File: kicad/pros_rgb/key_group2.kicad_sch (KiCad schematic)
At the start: 8 parts

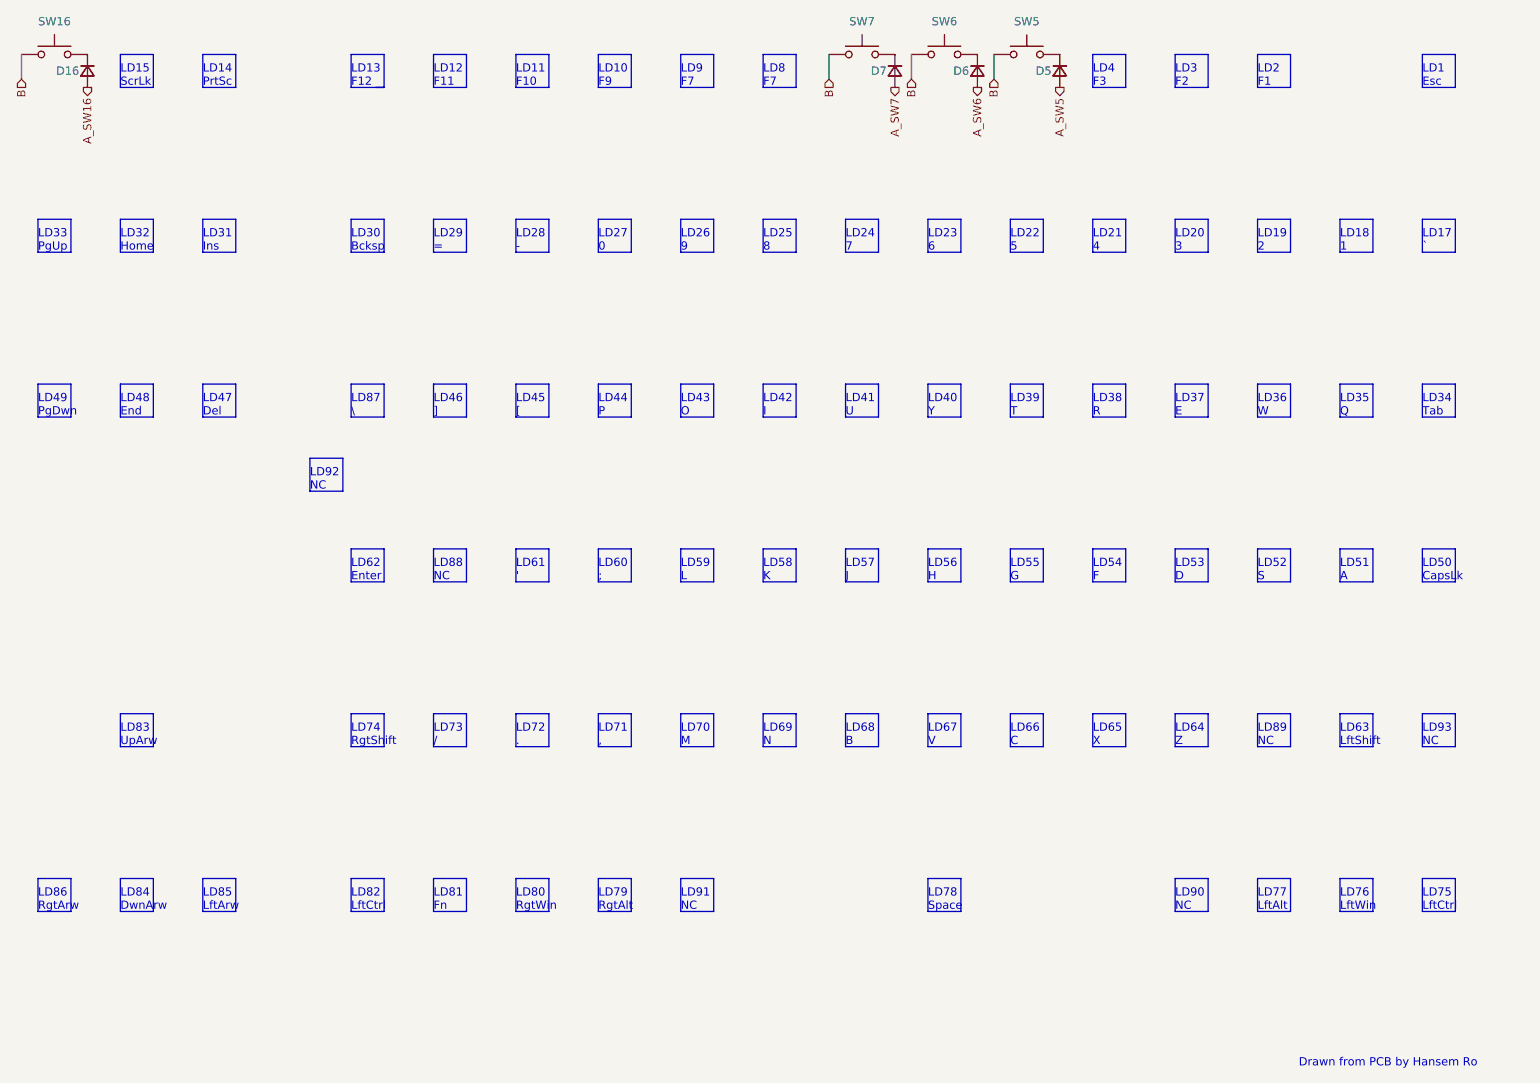
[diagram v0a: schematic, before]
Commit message: kicad/pros_rgb: update key groupings
These new groupings are based off ordering in firmware:
https://github.com/hansemro/pok3r_re_firmware/blob/4b68aa4baf7d28dc8dbf8eebcb1fdb59e7bcd629/disassemble/cmprosrgb/v122/cmprosrgb_v122.txt#L14599-L14629
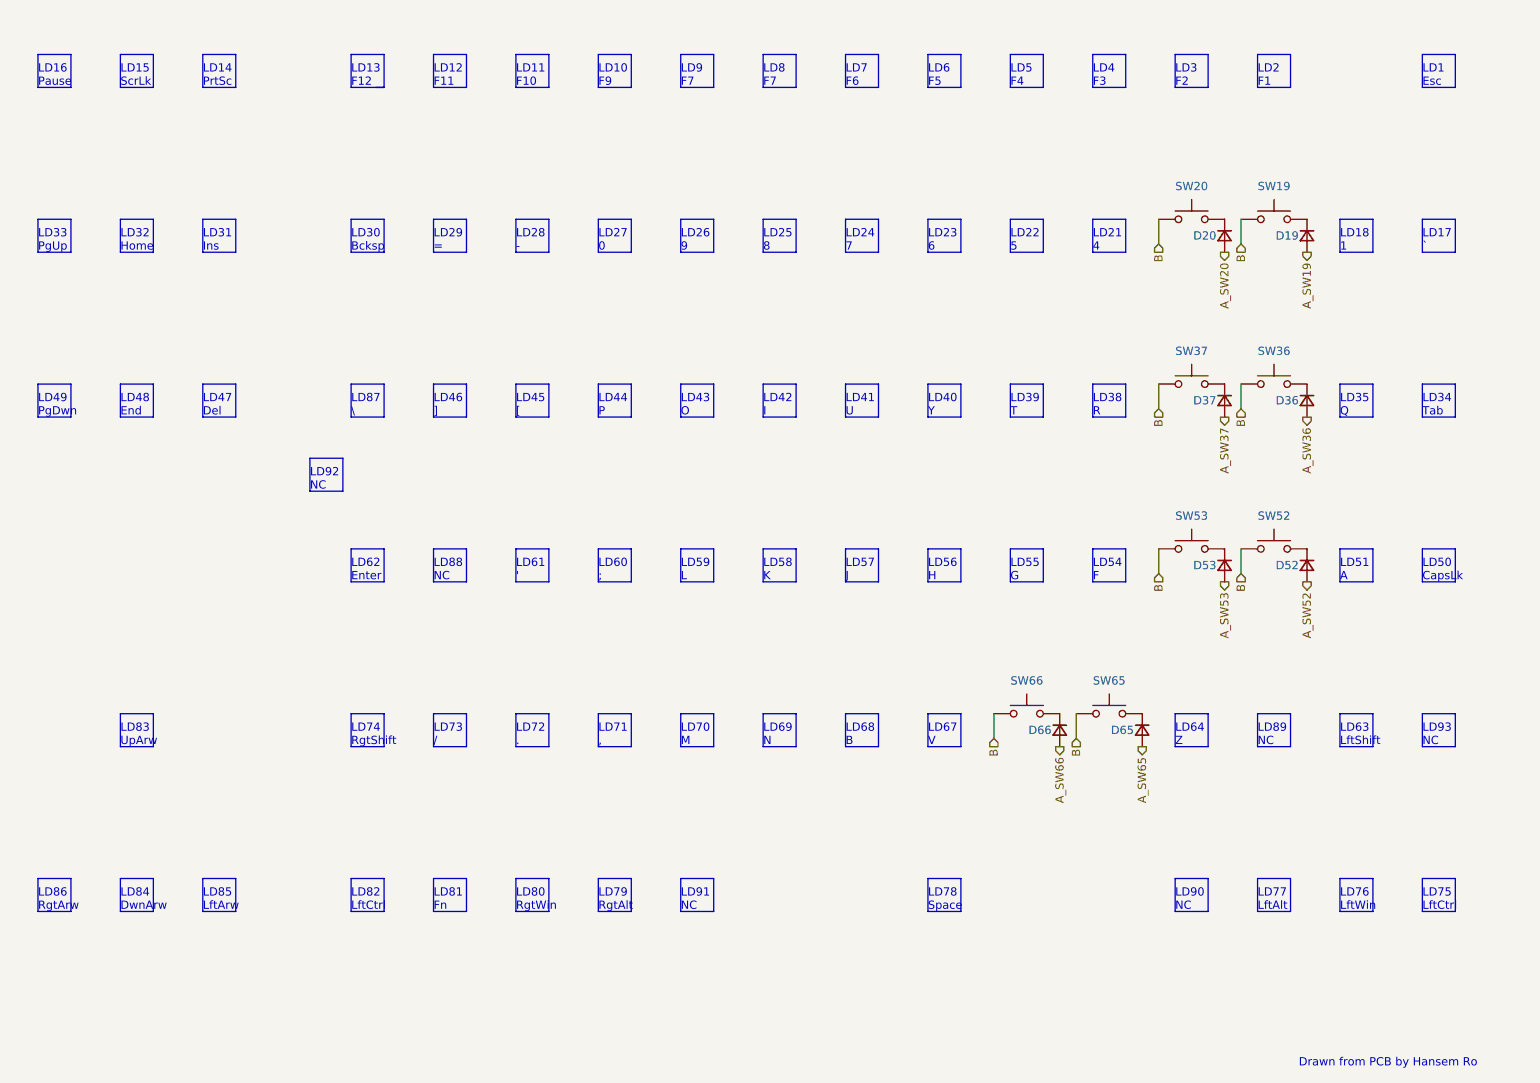
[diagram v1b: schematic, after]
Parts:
- removed D16, D5, D6, D7: ~, symbol Device:D_Small
- removed SW16, SW5, SW6, SW7: ~, symbol Switch:SW_Push
- added D19, D20, D36, D37, D52, D53, D65, D66: (no value), symbol Device:D_Small
- added SW19, SW20, SW36, SW37, SW52, SW53, SW65, SW66: (no value), symbol Switch:SW_Push
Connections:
- net B: now also SW19.1, SW20.1, SW36.1, SW37.1, SW52.1, SW53.1, SW65.1, SW66.1
- new net: D53.1 (K), SW53.2
- new net: D36.1 (K), SW36.2
- new net: D52.1 (K), SW52.2
- new net: D65.1 (K), SW65.2
- new net: D20.1 (K), SW20.2
- new net: D37.1 (K), SW37.2
- new net: D66.1 (K), SW66.2
- new net: D19.1 (K), SW19.2
- new net A_SW19: D19.2 (A)
- new net A_SW20: D20.2 (A)
- new net A_SW36: D36.2 (A)
- new net A_SW37: D37.2 (A)
- new net A_SW52: D52.2 (A)
- new net A_SW53: D53.2 (A)
- new net A_SW65: D65.2 (A)
- new net A_SW66: D66.2 (A)
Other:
- note added: "LD16 Pause"
- note added: "LD5 F4"
- note added: "LD6 F5"
- note added: "LD7 F6"
- note removed: "LD19 2"
- note removed: "LD20 3"
- note removed: "LD36 W"
- note removed: "LD37 E"
- note removed: "LD52 S"
- note removed: "LD53 D"
- note removed: "LD65 X"
- note removed: "LD66 C"

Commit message: kicad/pros_rgb: mark as Rev. B
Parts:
- D19, D20, D36, D37, D52, D53, D65, D66, SW19, SW20, SW36, SW37, SW52, SW53, SW65, SW66: value (none) -> ~
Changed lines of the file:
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@@
     (in_bom yes) (on_board yes)
     (property "Reference" "SW53" (id 0) (at 236.22 95.25 0))
-    (property "Value" "" (id 1) (at 236.22 95.25 0))
+    (property "Value" "~" (id 1) (at 236.22 95.25 0))
     (property "Footprint" "" (id 2) (at 236.22 95.25 0)
       (effects (font (size 1.27 1.27)) hide)
@@
       (effects (font (size 1.27 1.27)) (justify right))
     )
-    (property "Value" "" (id 1) (at 256.54 78.7399 90)
+    (property "Value" "~" (id 1) (at 256.54 78.7399 90)
       (effects (font (size 1.27 1.27)) (justify left))
     )
@@
       (effects (font (size 1.27 1.27)) (justify right))
     )
-    (property "Value" "" (id 1) (at 256.54 104.1399 90)
+    (property "Value" "~" (id 1) (at 256.54 104.1399 90)
       (effects (font (size 1.27 1.27)) (justify left))
     )
@@
       (effects (font (size 1.27 1.27)) (justify right))
     )
-    (property "Value" "" (id 1) (at 231.14 129.5399 90)
+    (property "Value" "~" (id 1) (at 231.14 129.5399 90)
       (effects (font (size 1.27 1.27)) (justify left))
     )
@@
       (effects (font (size 1.27 1.27)) (justify right))
     )
-    (property "Value" "" (id 1) (at 243.84 53.3399 90)
+    (property "Value" "~" (id 1) (at 243.84 53.3399 90)
       (effects (font (size 1.27 1.27)) (justify left))
     )
@@
     (in_bom yes) (on_board yes)
     (property "Reference" "SW36" (id 0) (at 248.92 69.85 0))
-    (property "Value" "" (id 1) (at 248.92 69.85 0))
+    (property "Value" "~" (id 1) (at 248.92 69.85 0))
     (property "Footprint" "" (id 2) (at 248.92 69.85 0)
       (effects (font (size 1.27 1.27)) hide)
@@
     (in_bom yes) (on_board yes)
     (property "Reference" "SW37" (id 0) (at 236.22 69.85 0))
-    (property "Value" "" (id 1) (at 236.22 69.85 0))
+    (property "Value" "~" (id 1) (at 236.22 69.85 0))
     (property "Footprint" "" (id 2) (at 236.22 69.85 0)
       (effects (font (size 1.27 1.27)) hide)
@@
     (in_bom yes) (on_board yes)
     (property "Reference" "SW66" (id 0) (at 210.82 120.65 0))
-    (property "Value" "" (id 1) (at 210.82 120.65 0))
+    (property "Value" "~" (id 1) (at 210.82 120.65 0))
     (property "Footprint" "" (id 2) (at 210.82 120.65 0)
       (effects (font (size 1.27 1.27)) hide)
@@
       (effects (font (size 1.27 1.27)) (justify right))
     )
-    (property "Value" "" (id 1) (at 243.84 78.7399 90)
+    (property "Value" "~" (id 1) (at 243.84 78.7399 90)
       (effects (font (size 1.27 1.27)) (justify left))
     )
@@
     (in_bom yes) (on_board yes)
     (property "Reference" "SW19" (id 0) (at 248.92 44.45 0))
-    (property "Value" "" (id 1) (at 248.92 44.45 0))
+    (property "Value" "~" (id 1) (at 248.92 44.45 0))
     (property "Footprint" "" (id 2) (at 248.92 44.45 0)
       (effects (font (size 1.27 1.27)) hide)
@@
       (effects (font (size 1.27 1.27)) (justify right))
     )
-    (property "Value" "" (id 1) (at 256.54 53.3399 90)
+    (property "Value" "~" (id 1) (at 256.54 53.3399 90)
       (effects (font (size 1.27 1.27)) (justify left))
     )
@@
     (in_bom yes) (on_board yes)
     (property "Reference" "SW20" (id 0) (at 236.22 44.45 0))
-    (property "Value" "" (id 1) (at 236.22 44.45 0))
+    (property "Value" "~" (id 1) (at 236.22 44.45 0))
     (property "Footprint" "" (id 2) (at 236.22 44.45 0)
       (effects (font (size 1.27 1.27)) hide)
@@
       (effects (font (size 1.27 1.27)) (justify right))
     )
-    (property "Value" "" (id 1) (at 243.84 104.1399 90)
+    (property "Value" "~" (id 1) (at 243.84 104.1399 90)
       (effects (font (size 1.27 1.27)) (justify left))
     )
@@
     (in_bom yes) (on_board yes)
     (property "Reference" "SW52" (id 0) (at 248.92 95.25 0))
-    (property "Value" "" (id 1) (at 248.92 95.25 0))
+    (property "Value" "~" (id 1) (at 248.92 95.25 0))
     (property "Footprint" "" (id 2) (at 248.92 95.25 0)
       (effects (font (size 1.27 1.27)) hide)
@@
     (in_bom yes) (on_board yes)
     (property "Reference" "SW65" (id 0) (at 223.52 120.65 0))
-    (property "Value" "" (id 1) (at 223.52 120.65 0))
+    (property "Value" "~" (id 1) (at 223.52 120.65 0))
     (property "Footprint" "" (id 2) (at 223.52 120.65 0)
       (effects (font (size 1.27 1.27)) hide)
@@
       (effects (font (size 1.27 1.27)) (justify right))
     )
-    (property "Value" "" (id 1) (at 218.44 129.5399 90)
-      (effects (font (size 1.27 1.27)) (justify left))
-    )
+    (property "Value" "~" (id 1) (at 218.44 129.5399 90)
+      (effects (font (size 1.27 1.27)) (justify left))
+    )

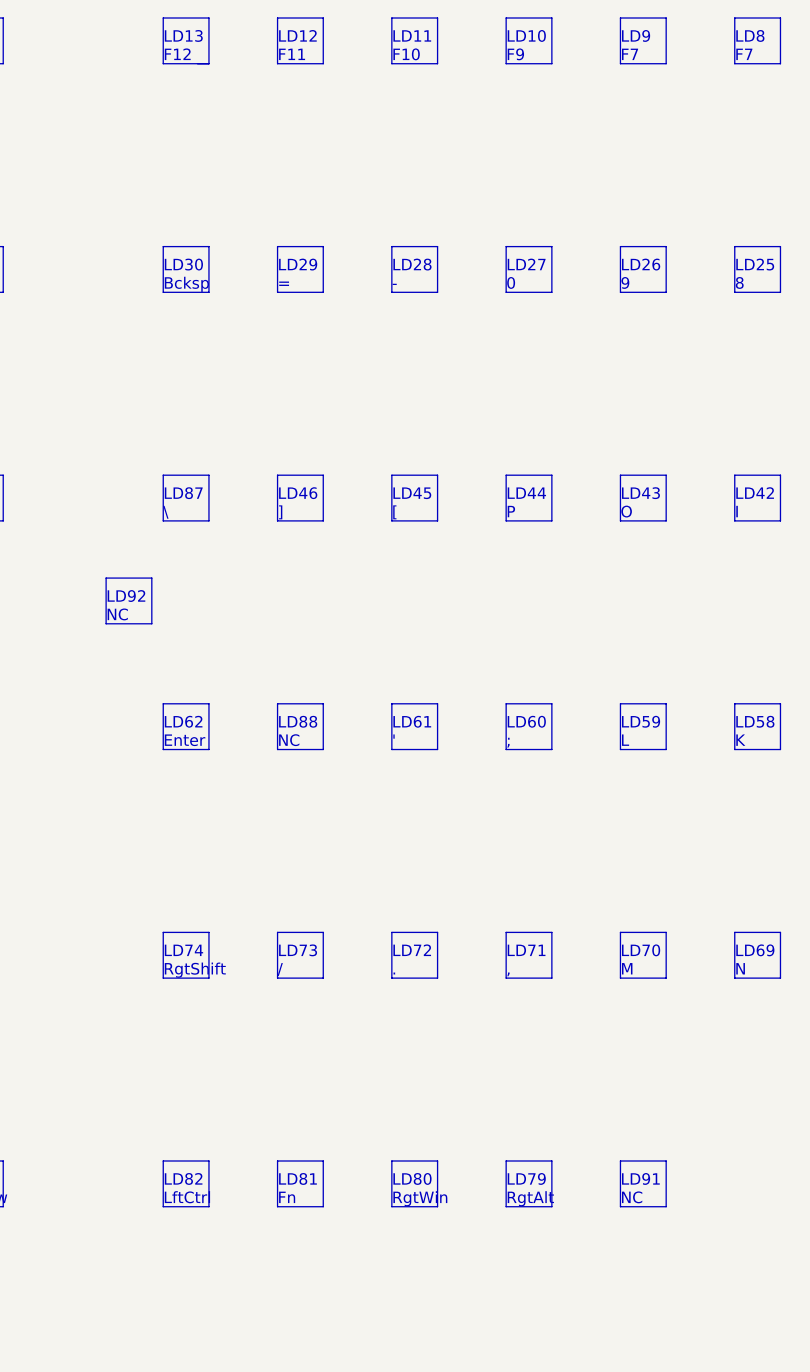
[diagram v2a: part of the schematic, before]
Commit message: kicad/pros_rgb: fix typos
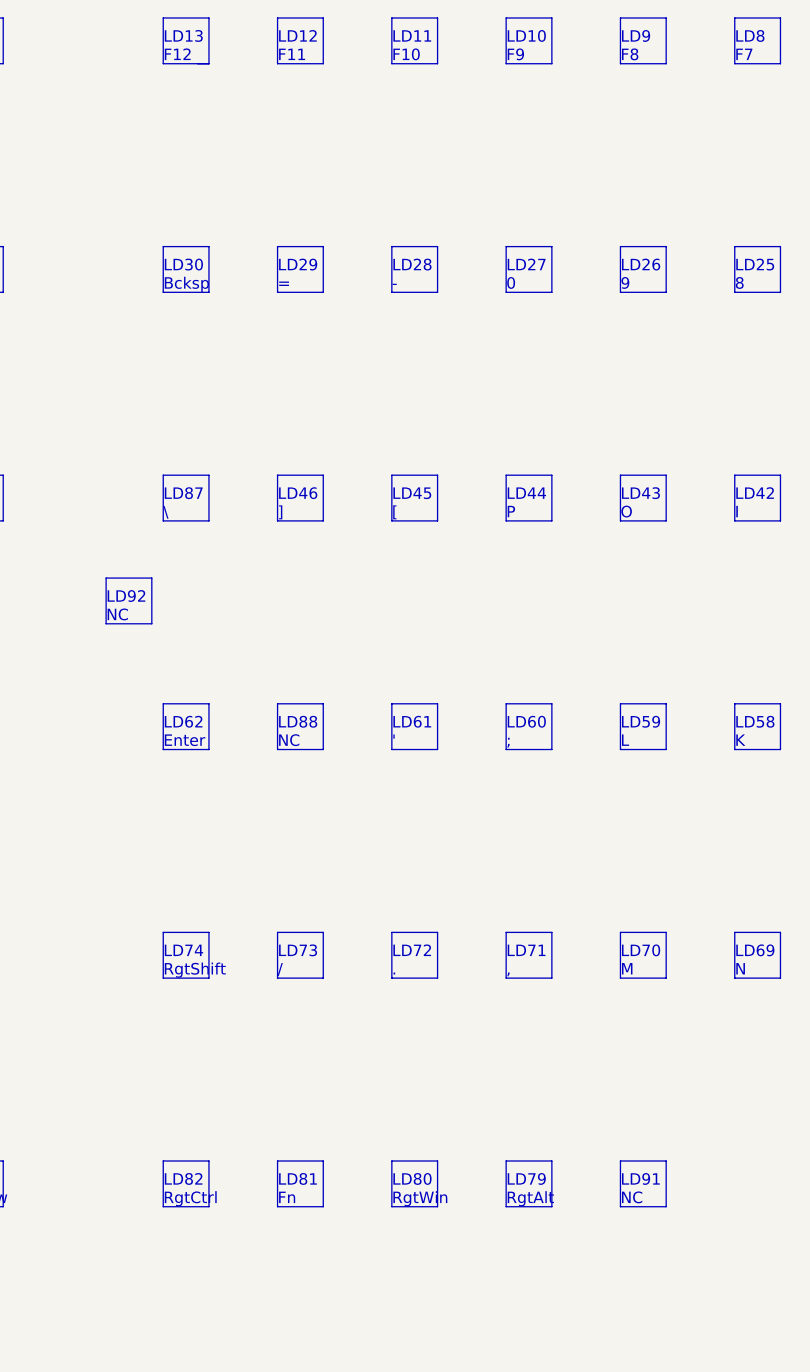
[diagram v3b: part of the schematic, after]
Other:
- note added: "LD82 RgtCtrl"
- note added: "LD9 F8"
- note removed: "LD82 LftCtrl"
- note removed: "LD9 F7"
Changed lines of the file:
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@@
     (effects (font (size 1.27 1.27)) (justify left bottom))
   )
-  (text "LD9\nF7" (at 157.48 29.21 0)
+  (text "LD9\nF8" (at 157.48 29.21 0)
     (effects (font (size 1.27 1.27)) (justify left bottom))
   )
@@
     (effects (font (size 1.27 1.27)) (justify left bottom))
   )
-  (text "LD82\nLftCtrl" (at 106.68 156.21 0)
+  (text "LD82\nRgtCtrl" (at 106.68 156.21 0)
     (effects (font (size 1.27 1.27)) (justify left bottom))
   )
